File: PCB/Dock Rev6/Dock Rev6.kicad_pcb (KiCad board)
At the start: 2 copper layers, 45 x 94 mm, 29 parts, among them J1 HX-XH2.54-2PZZ, Q1 FS8205A, SW1 KH-6X6X5H-ZJ, U1 ESP32-C3 Super Mini, U2 CC1101 433MHz COIL

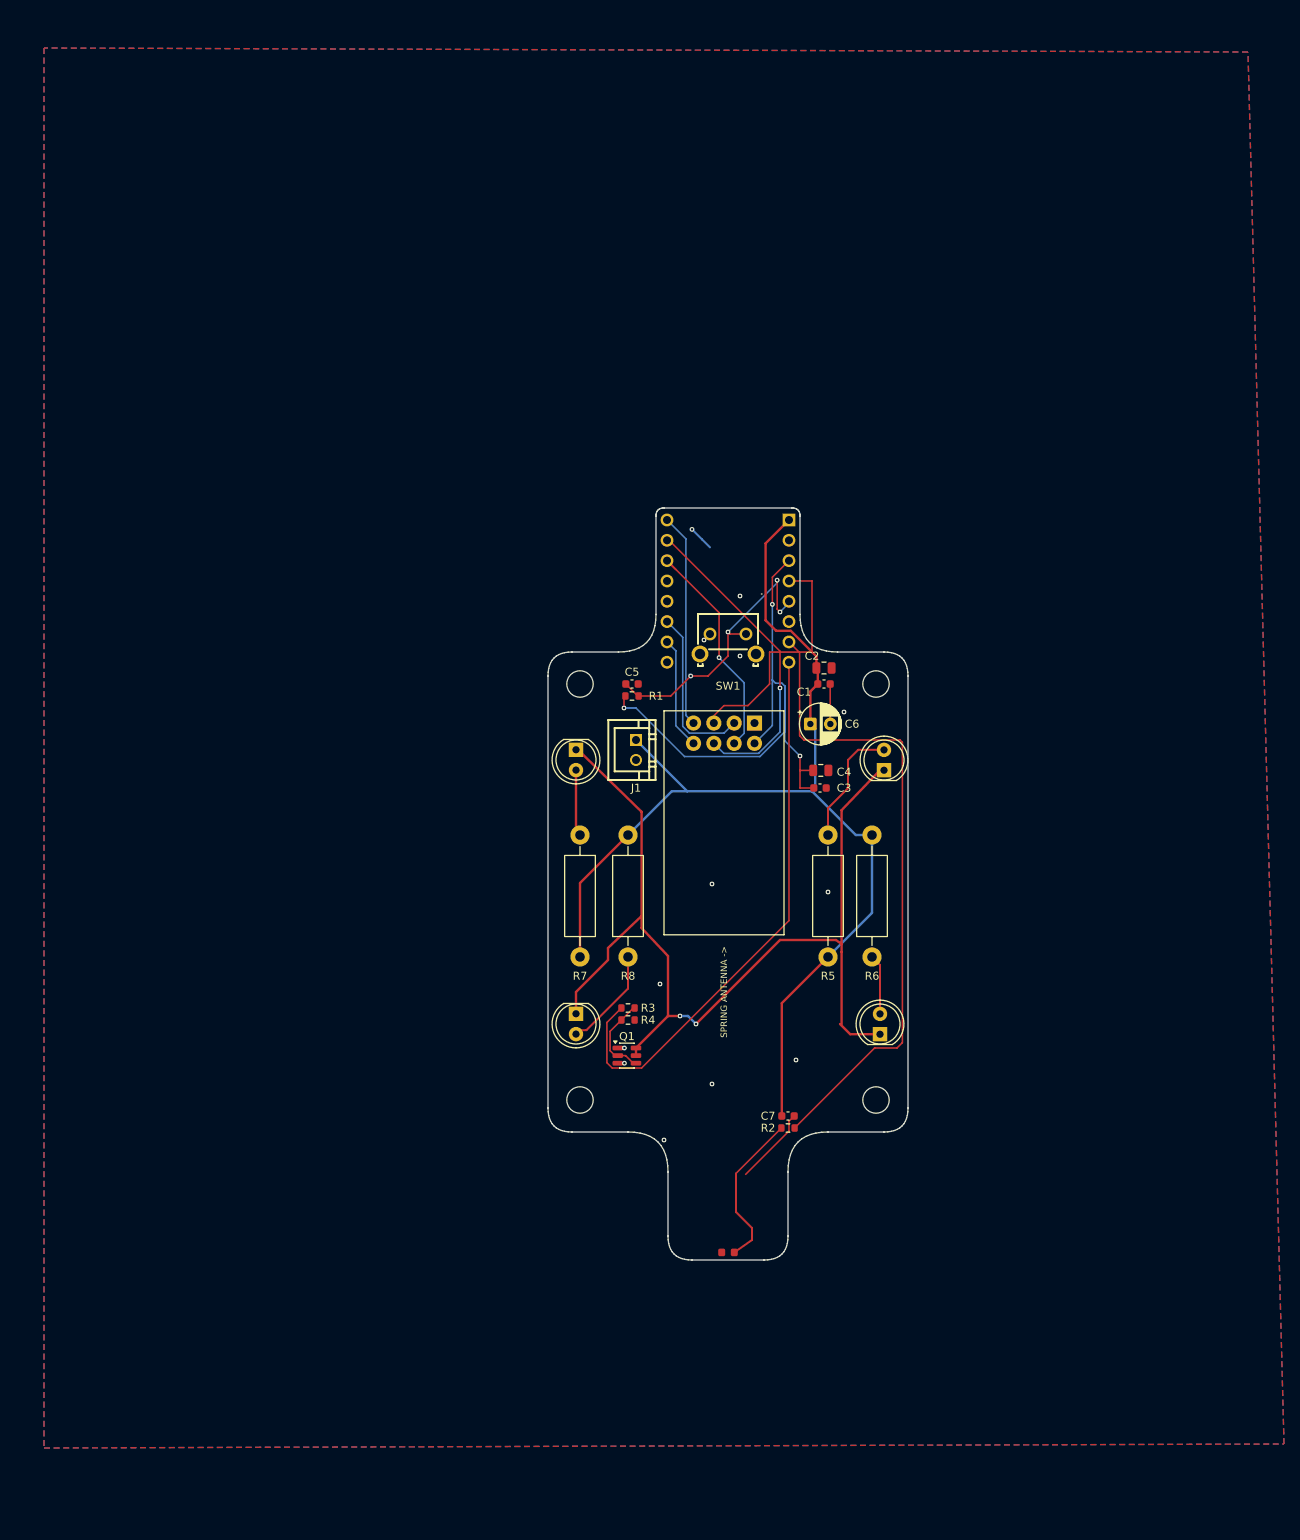
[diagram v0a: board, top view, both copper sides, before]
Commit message: Merge MIC_VDD with IO45 net and regenerate Rev6 gerbers
Schematic:
- Added the missing 10.16 mm wire from (281.94, 69.85) to the MIC_VDD
  global label at (292.10, 69.85). The label had been drawn but never
  landed on the net, so MIC_VDD and Net-(D3-A) were two separate nets
  joined only by a track physically overlapping U7 pad 26 and D3 pad 2.
- MIC_VDD now carries D3.2, MIC1.2 and U7.26 (IO45); Net-(D3-A) is gone.

PCB:
- Netlist re-imported; MIC1 pin 6 grounded via a track to a new GND via
  at (145.50, 104.50) landing in the B.Cu plane; MIC_VDD routed properly.
- DRC errors 51 -> 44: all 4 shorting_items cleared, solder_mask_bridge
  9 -> 4 (remaining four are the fiducials).
- Regenerated gerber.zip from the current board (kicad-cli 10.0.4).
  Changes confined to F.Cu, B.Cu and one new PTH via; silkscreen, mask,
  paste and edge cuts are byte-identical to the previous set.

Also adds Dock Rev6 production files and the pogo-pin case STL.

Known outstanding: 11 clearance violations remain in the J7 5V-in and
J3 battery routing, tightest 0.100 mm, below JLCPCB's 0.127 mm minimum.
CPL.csv and BOM.xlsx are unchanged and still need regeneration.

Co-Authored-By: Claude Opus 5 <noreply@anthropic.com>
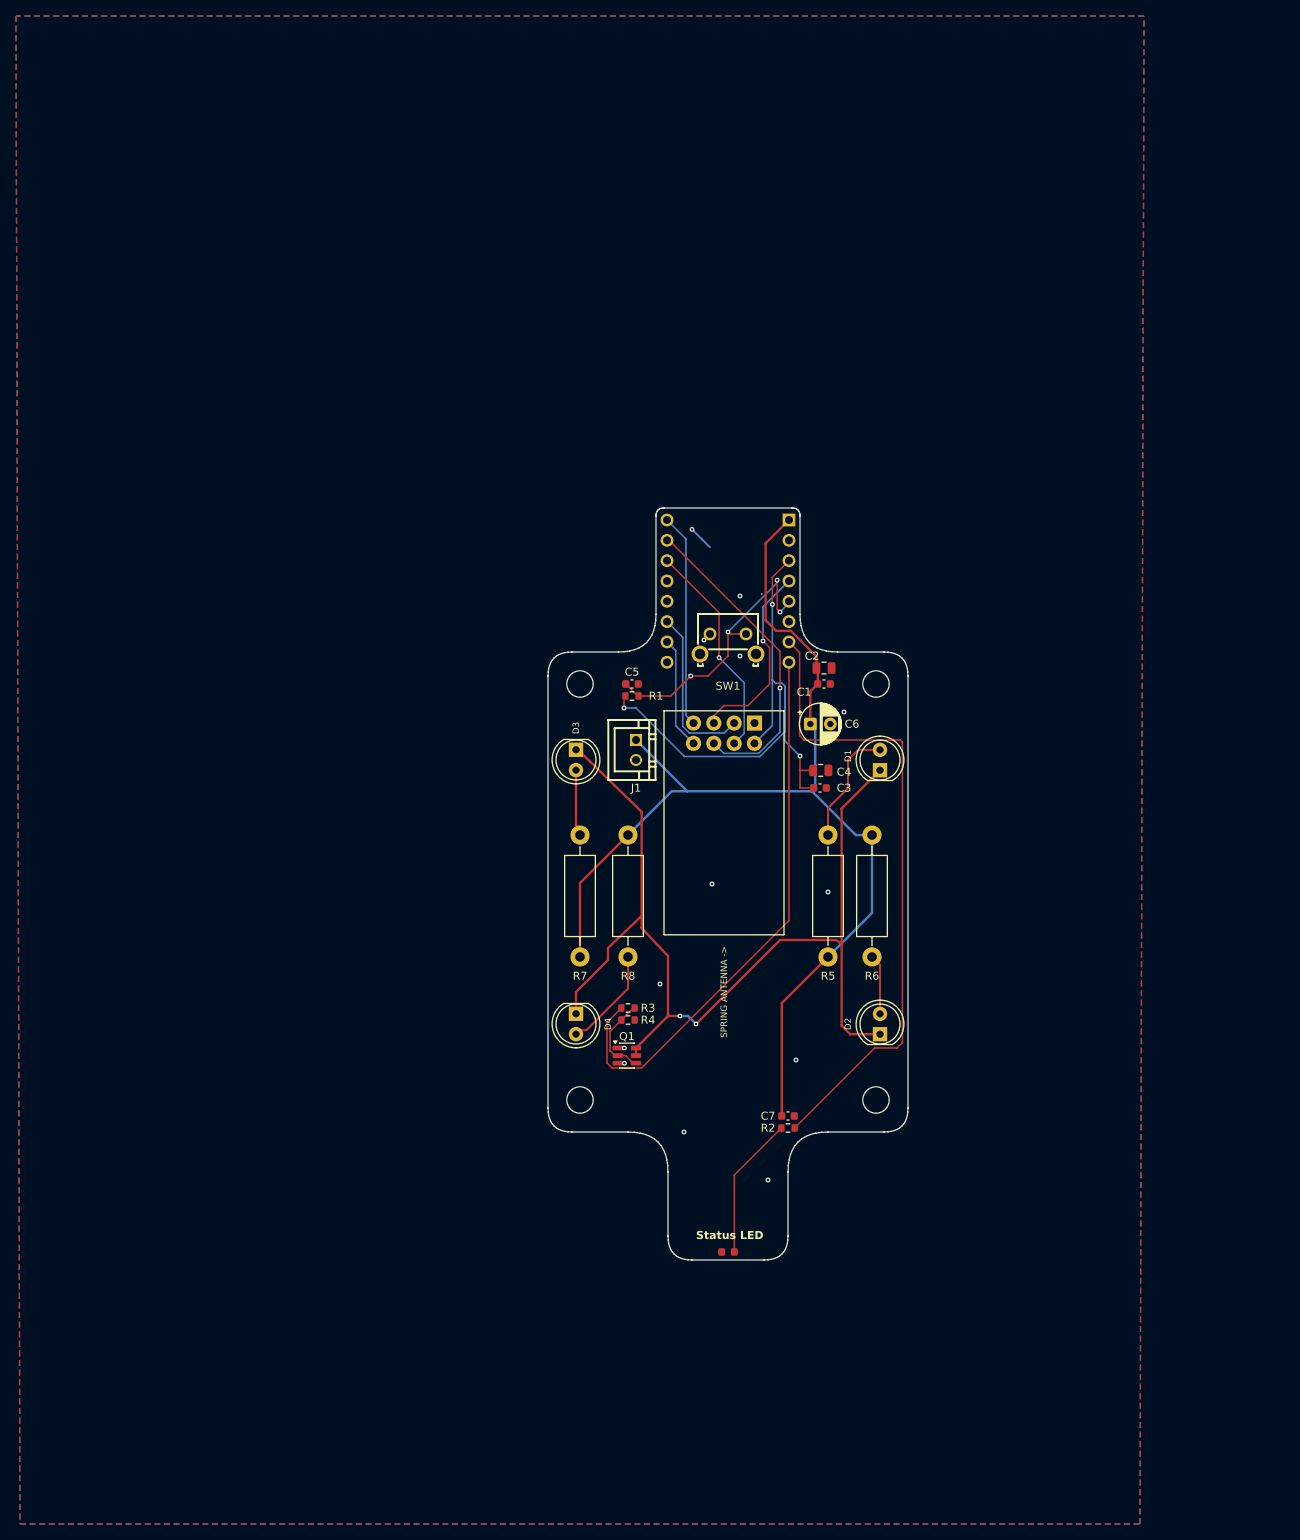
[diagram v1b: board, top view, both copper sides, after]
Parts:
- moved D1 0.50 mm to (119.0, 104.8)
- moved D5 0.05 mm to (100.0, 165.0)
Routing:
- net GND: track 19.7 -> 5.15 mm
- net RF_SCK: track 30.6 -> 24.1 mm, vias 0 -> 1
- net RF_CSN: track 28.9 -> 27.4 mm
- net Net-(D5-A): track 19.9 -> 18.8 mm
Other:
- board text added: "Status LED"

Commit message: Restructure CAD around display variants, publish the Rev6 charging dock
CAD is now organised by what you print rather than by revision:

  CAD/Adafruit LCD/    3MF + STL set for the original Adafruit screen
  CAD/BuyDisplay LCD/  3MF + STL set for the EastRising/BuyDisplay screen
  CAD/Dock/            dock shell, base lid, menu button + 3MF
  CAD/*.f3z            current Fusion sources (remote v37/v38, dock v47)

The old CAD/Case Rev6 and CAD/Dock Rev6 trees are gone; their current
content is superseded by the v37/v47 exports. FusionScripts, Hardware
Models and PCB Imports keep their existing paths under CAD/.

Charging dock, published for the first time:
- Fusion source, printable parts and a Bambu 3MF
- KiCad project already present, now with a production set beside the
  gerbers: CPL.csv and a new BOM.xlsx
- README gains a Charging dock section covering pogo-pin charging, the
  ESP32-C3, the four-emitter IR bank, the CC1101 433 MHz radio and the
  power options

The dock BOM is generated from the board: 25 parts in 16 grouped lines,
matching the 25 CPL rows. LCSC codes come from the dock's own README
(C405273, C908265, C42391660, C2837541), from the PCB (C965807), and for
four passives from the remote BOM where value and footprint match exactly
(C1591, C15850, C22548, C98220). Ten designators still have no code -
100R, 100k, 100uF, the 39R IR resistors, and the two owner-supplied
modules - and are left blank rather than guessed.

Dock PCB sources also updated, plus the pre-FS8205A-fix board snapshots.

Note: CAD/Case Rev6/Community Parts (Case-Bulky-Bottom and the TPU
small-button variants) no longer exists on the source drive and is
removed here too. Restore with:
  git checkout 95b55f4 -- "CAD/Case Rev6/Community Parts"

Co-Authored-By: Claude Opus 5 <noreply@anthropic.com>
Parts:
- moved C7 20.5 mm to (87.5, 143.5)
- moved R2 15.9 mm to (100.0, 163.5), turned to 0 degrees
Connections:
- Q1 pad 2: IR_GATE -> IR_K
- Q1 pad 6: IR_K -> IR_GATE
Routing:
- net Net-(U1-GPIO1/A1): track 80.9 -> 98.8 mm
- net Net-(D5-A): track 18.8 -> 1.52 mm
- net IR_K: track 125.8 -> 134.9 mm, vias 2 -> 3
- net +5V: track 141.4 -> 139.2 mm
- net IR_GATE: track 10.6 -> 11.5 mm, vias 0 -> 3
- net GND: track 5.15 -> 5.89 mm, vias 13 -> 15
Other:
- board text added: "OpenRemote Dock Rev6 Firmware 1.30+ Phillip Carlson Sep 2026"

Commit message: Tidy the dock project and add D6 pogo-output protection diode
Cleanup - removed 21 files, keeping only the current board and
schematic. Everything remains in git history for rollback:
- 14 Dock Rev6.before-* rollback boards, schematics and prl
- Dock Rev6 Component Staging Backup.kicad_pcb
- 4 DRC/ERC/parity report files
- Dock Rev6.net and the exported Dock Rev6 Schematic.pdf

New diode, schematic only:
- D6, BAT20J Schottky, LCSC C49238173 - the same part as the remote's D1
- In series between +5V and J1 pin 1, creating the POGO_5V net, so the
  IR bank, ESP32 and decoupling stay on the raw 5V rail
- Orientation verified through the exported netlist: +5V carries D6 pin 2
  (A_2, anode) and POGO_5V carries D6 pin 1 (K_1, cathode) to J1 pin 1
- ERC passes with 0 violations

Deliberately NOT placed on the PCB - that is left to the owner.

Footprint and 3D model, project-local to match the dock's convention:
- project_libraries/footprints/DockRev6.pretty/D_SOD-323.kicad_mod
- project_libraries/3D-models/D_SOD-323.step
The footprint's model path is rewritten to ${KIPRJMOD}, so the project
does not depend on the global KiCad 3D model directory. The Diode symbol
library is added to sym-lib-table for the MBR0520 Schottky symbol, which
is what the remote uses for the same part.

The dock PCB also carries the owner's in-progress ESP32-C3 footprint
correction, untouched here.

Two caveats are recorded in the dock README: a series diode does not
limit current into a shorted pogo pair, and a BAT20J in SOD-323 is
marginal at the remote's ~1 A charge current.

Co-Authored-By: Claude Opus 5 <noreply@anthropic.com>
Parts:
- U1: moved to F.Cu
- turned U1 to 0 degrees
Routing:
- net Net-(U1-GPIO1/A1): track 98.8 -> 127.7 mm
- net +3V3: track 74.6 -> 58.0 mm, vias 3 -> 1
- net RF_MOSI: track 39.9 -> 29.5 mm, vias 1 -> 0
- net RF_GDO2: track 14.1 -> 23.1 mm, vias 0 -> 1
- net RF_MISO: track 26.8 -> 35.4 mm, vias 0 -> 4
- net BUTTON: track 36.1 -> 30.0 mm, vias 4 -> 1
- net IR_PWM: track 70.6 -> 65.6 mm
- net RF_GDO0: track 21.2 -> 25.8 mm
- net +5V: track 139.2 -> 143.0 mm
- net IR_K: track 134.9 -> 131.9 mm
- net GND: track 5.89 -> 2.97 mm, vias 15 -> 37
- net RF_SCK: track 24.1 -> 22.3 mm, vias 1 -> 0
- net RF_CSN: track 27.4 -> 28.8 mm, vias 1 -> 0
